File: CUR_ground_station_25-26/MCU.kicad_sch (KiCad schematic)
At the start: 14 parts, among them J4 Conn_01x04_Pin, SW7 PTS815SJM250SMTRLFS, SW8 PTS815SJM250SMTRLFS, U1 ESP32-S3-MINI-1

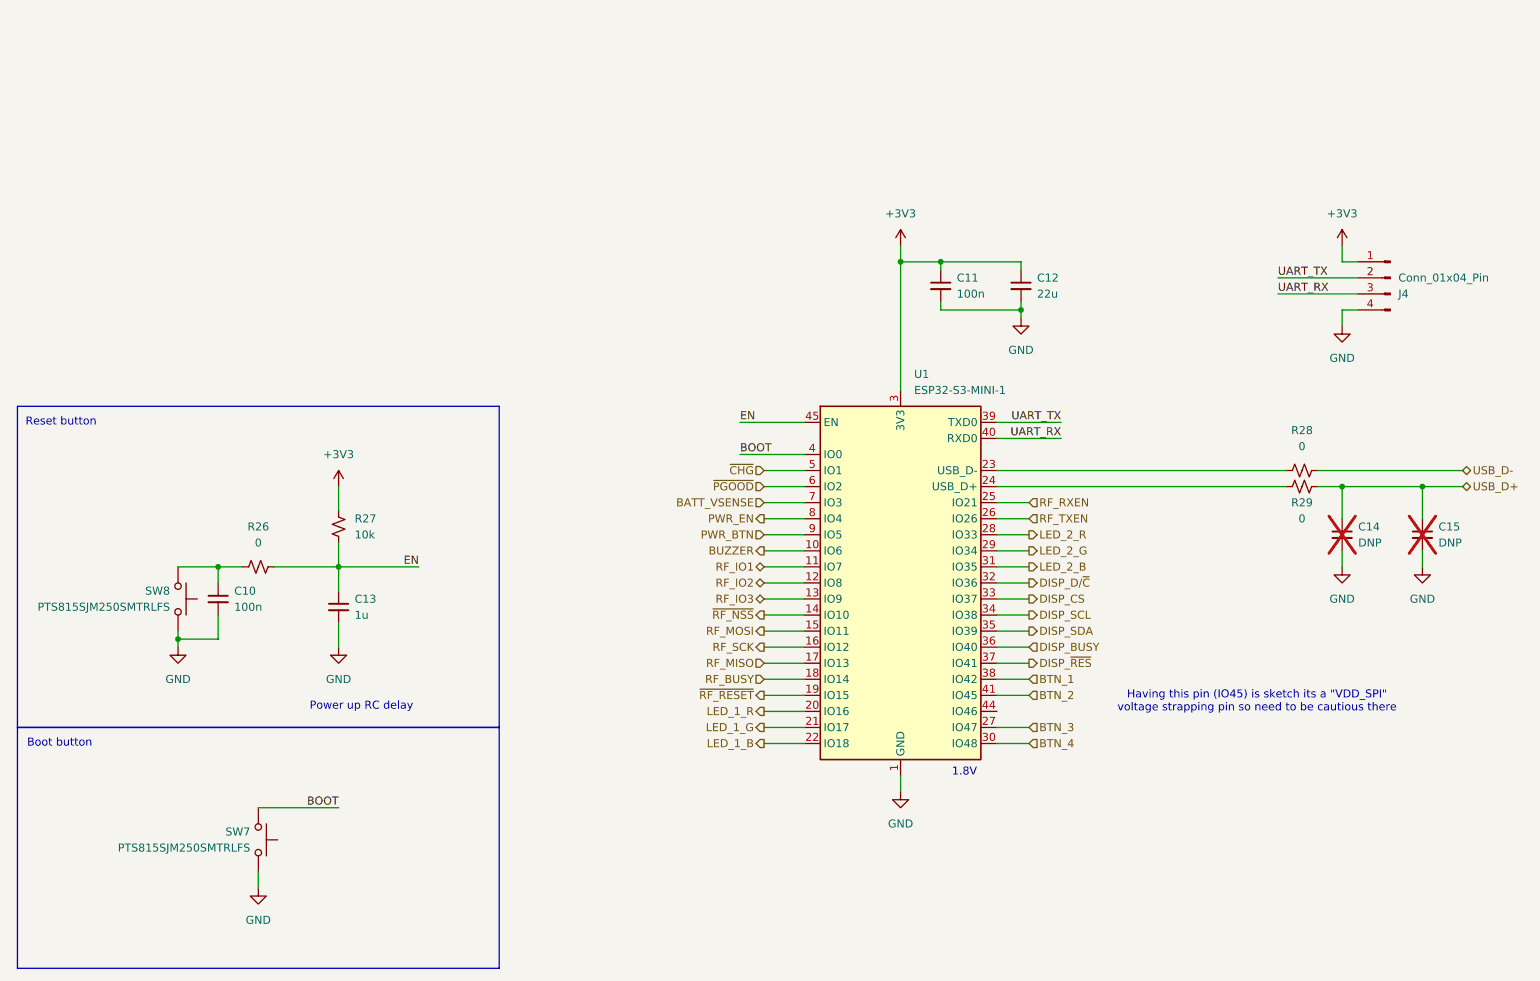
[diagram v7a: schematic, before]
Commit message: BOM optimization
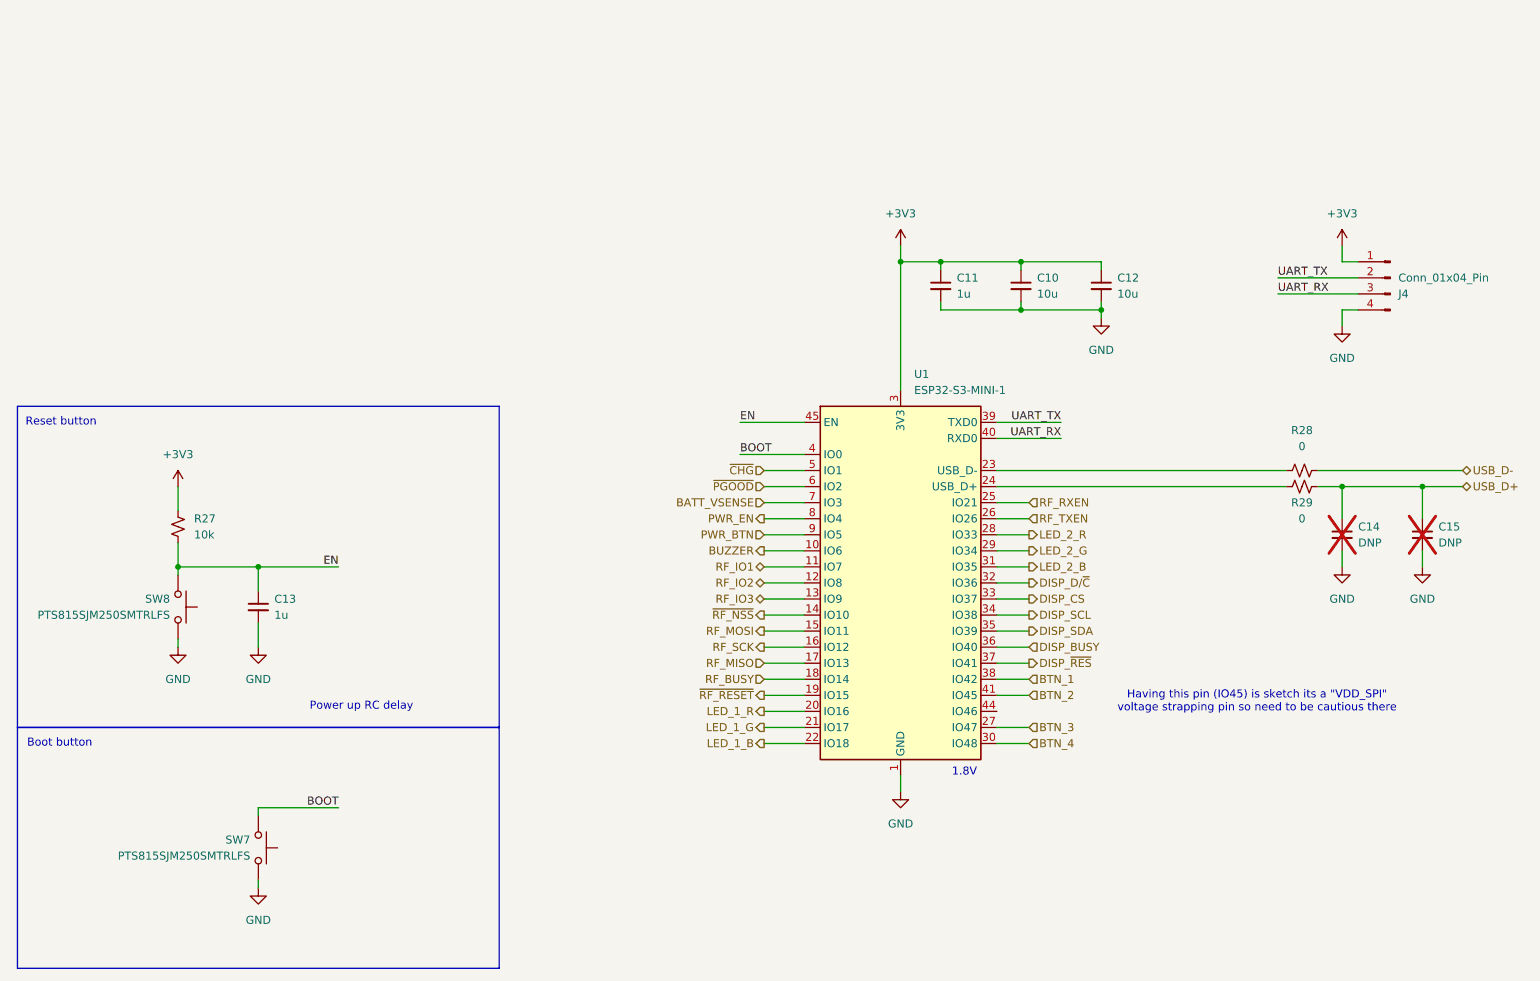
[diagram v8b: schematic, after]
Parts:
- removed R26: 0, Resistor_SMD:R_0603_1608Metric, symbol Device:R_Small_US
- C10: value 100n -> 10u
- C11: value 100n -> 1u
- C12: value 22u -> 10u
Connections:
- net +3V3: now also C10.1
- net EN: now also SW8.2
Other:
- moved on the sheet: C13, R27, SW7, SW8
